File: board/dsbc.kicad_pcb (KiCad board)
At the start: 2 copper layers, 28 parts, among them J1 DB15_Female_HighDensity, J2 Conn_02x20_Odd_Even, J3 Conn_02x20_Odd_Even, U1 W65C816S6PG-14, U2 25LCxxx

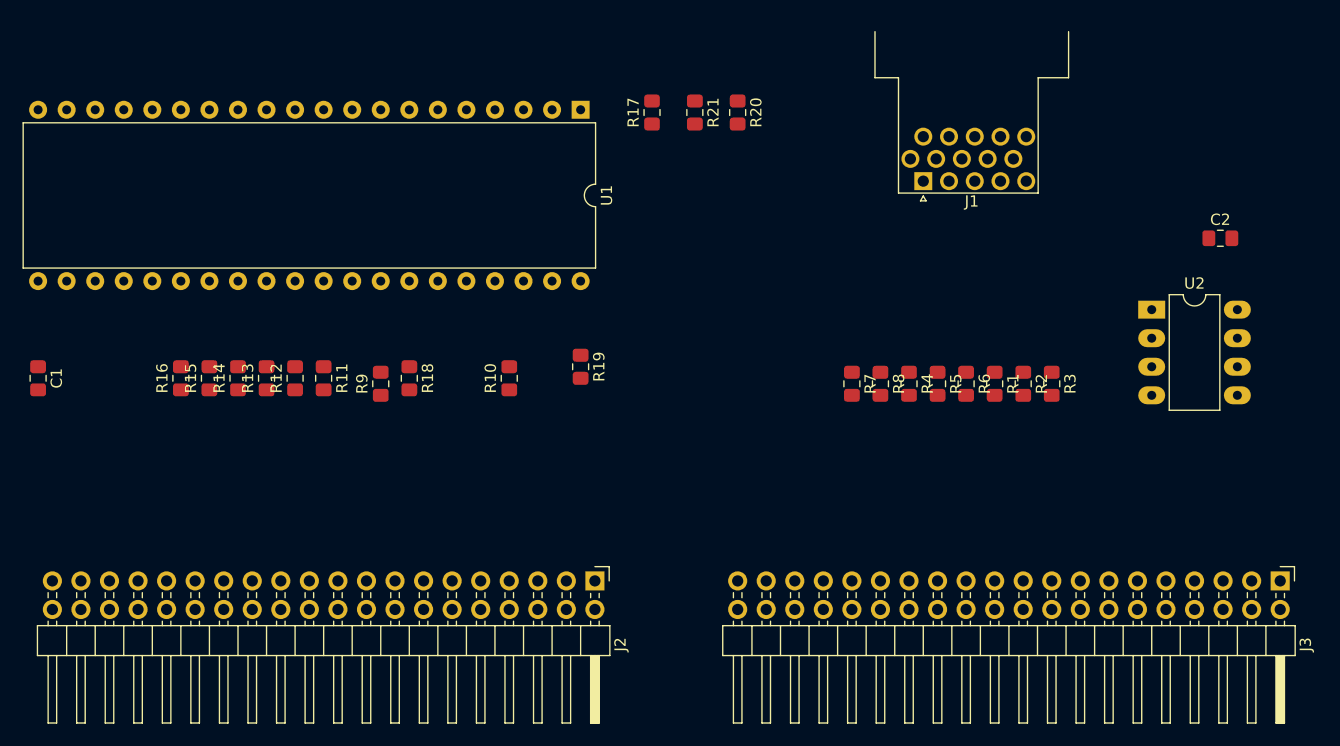
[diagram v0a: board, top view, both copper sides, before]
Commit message: board: placement. pin headers have wrong orientation
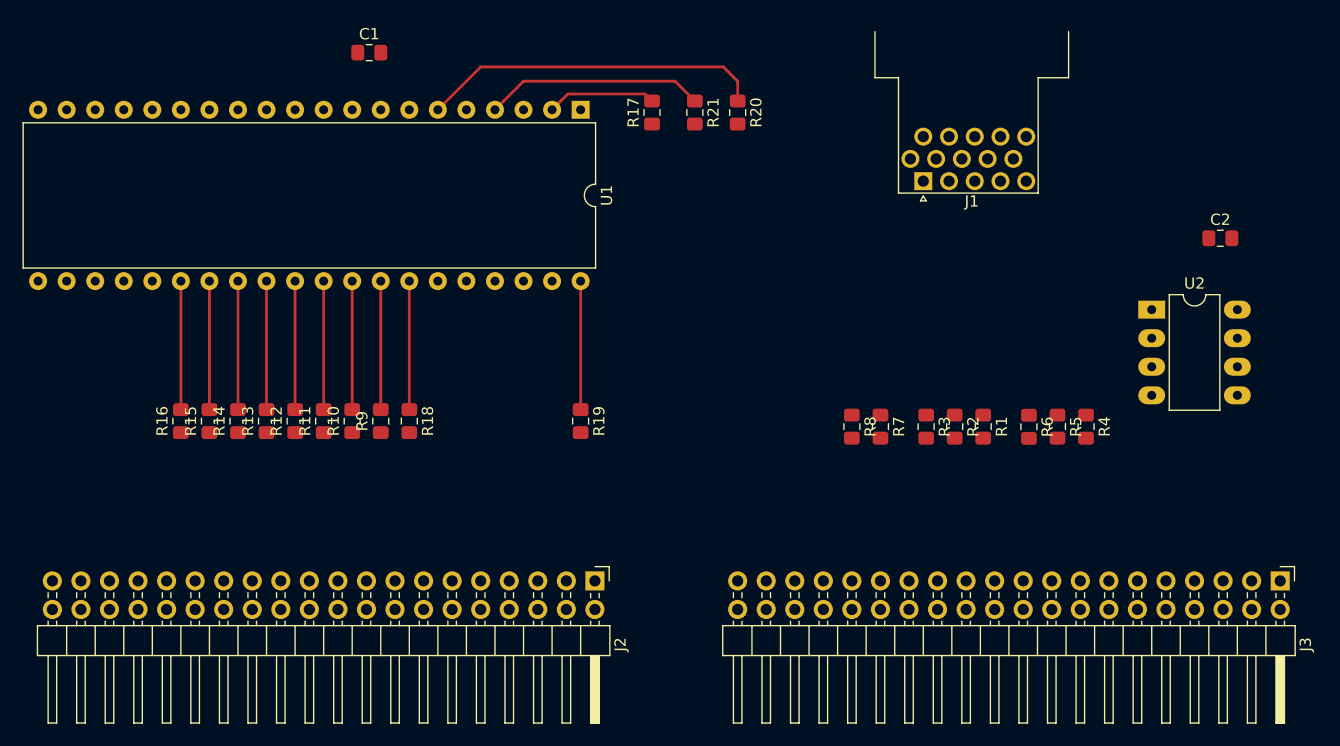
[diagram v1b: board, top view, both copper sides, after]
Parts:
- moved C1 41.3 mm to (93.0, 83.8), turned to 0 degrees
- moved R4 16.2 mm to (156.7, 117.1)
- moved R10 14.5 mm to (91.4, 116.6)
- moved R3 11.8 mm to (142.5, 117.1)
- moved R5 11.3 mm to (154.2, 117.1)
- moved R2 7.19 mm to (145.0, 117.1)
- moved R6 6.77 mm to (151.6, 117.1)
- moved R19 4.83 mm to (111.8, 116.6)
- moved R7 4.58 mm to (138.4, 117.1)
- moved R8 4.58 mm to (135.9, 117.1)
- moved R1 3.94 mm to (147.6, 117.1)
- moved R11 3.81 mm to (88.9, 116.6), turned to 90 degrees
- moved R12 3.81 mm to (86.4, 116.6)
- moved R13 3.81 mm to (83.8, 116.6)
- moved R14 3.81 mm to (81.3, 116.6)
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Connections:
- J3 pad 17: /G0 -> /R0
- J3 pad 18: /R0 -> /R1
- J3 pad 19: /G1 -> /R2
- J3 pad 20: /R1 -> /G0
- J3 pad 21: /G2 -> /G1
- J3 pad 22: /R2 -> /G2
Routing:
- net /~NMI: track 0.00 -> 30.5 mm
- net /~IRQ: track 0.00 -> 19.6 mm
- net Net-(R9-Pad2): track 0.00 -> 11.4 mm
- net Net-(R16-Pad2): track 0.00 -> 11.4 mm
- net Net-(R15-Pad2): track 0.00 -> 11.4 mm
- net Net-(R14-Pad2): track 0.00 -> 11.4 mm
- net Net-(R13-Pad2): track 0.00 -> 11.4 mm
- net Net-(R12-Pad2): track 0.00 -> 11.4 mm
- net Net-(R11-Pad2): track 0.00 -> 11.4 mm
- net Net-(R10-Pad2): track 0.00 -> 11.4 mm
- net /~RESET_CPU: track 0.00 -> 11.4 mm
- net /R~W: track 0.00 -> 11.4 mm
- net Net-(R17-Pad2): track 0.00 -> 9.73 mm
